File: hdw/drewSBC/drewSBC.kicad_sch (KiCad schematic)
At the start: 0 parts

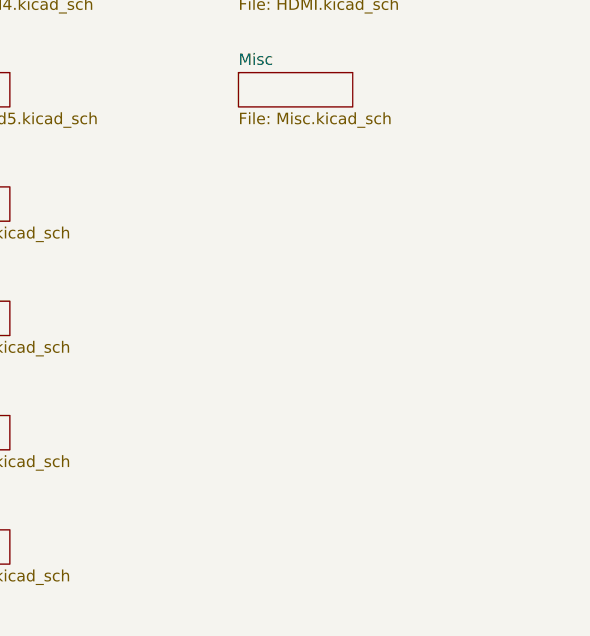
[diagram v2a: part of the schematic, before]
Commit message: ripped up ETH phy
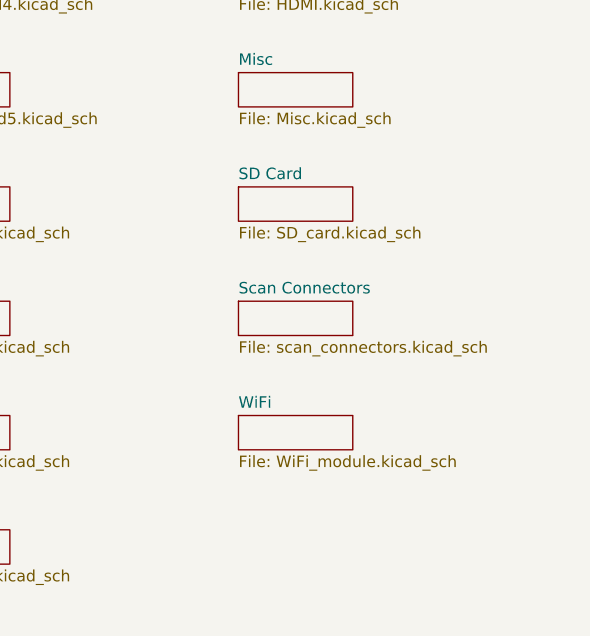
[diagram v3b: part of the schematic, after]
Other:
- added sheet SD Card (SD_card.kicad_sch)
- added sheet Scan Connectors (scan_connectors.kicad_sch)
- added sheet WiFi (WiFi_module.kicad_sch)

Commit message: more GB Ethernet work
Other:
- sheet HDMI renamed HDMI_Output
- added sheet Ethernet Support (Ethernet_Support.kicad_sch)
- sheet HDMI_Output: file HDMI.kicad_sch -> HDMI_Output.kicad_sch
